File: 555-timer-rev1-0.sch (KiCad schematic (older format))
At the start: 10 parts, among them J1 Conn_01x02_Female, U1 SA555D

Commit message: Add bistable reset switch to schematic.
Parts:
- added JP?: SolderJumper_2_Open, Jumper:SolderJumper-2_P1.3mm_Open_TrianglePad1.0x1.5mm, symbol Jumper:SolderJumper_2_Open
- added R?: 220, Resistor_SMD:R_1206_3216Metric_Pad1.42x1.75mm_HandSolder, symbol Device:R
- added SW?: SW_Push, symbol Switch:SW_Push
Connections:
- net +5V: now also R?.1; no longer U1.4 (R)
- net GND: now also SW?.1
- new net: JP?.1 (A), R?.2, U1.4 (R)
- new net: JP?.2 (B), SW?.2
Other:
- moved on the sheet: C2
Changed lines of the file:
@@
 L Device:C C2
 U 1 1 5F27D81E
-P 4850 4450
-F 0 "C2" H 4965 4496 50  0000 L CNN
-F 1 "100pF" H 4965 4405 50  0000 L CNN
-F 2 "Capacitor_SMD:C_1206_3216Metric_Pad1.42x1.75mm_HandSolder" H 4888 4300 50  0001 C CNN
-F 3 "~" H 4850 4450 50  0001 C CNN
-	1    4850 4450
+P 4650 4450
+F 0 "C2" H 4765 4496 50  0000 L CNN
+F 1 "100pF" H 4765 4405 50  0000 L CNN
+F 2 "Capacitor_SMD:C_1206_3216Metric_Pad1.42x1.75mm_HandSolder" H 4688 4300 50  0001 C CNN
+F 3 "~" H 4650 4450 50  0001 C CNN
+	1    4650 4450
 	1    0    0    -1
 $EndComp
@@
 $EndComp
 Wire Wire Line
-	6000 3600 6000 3150
-Wire Wire Line
 	8050 5050 8050 5250
 Wire Wire Line
 	6500 4000 6750 4000
-Wire Wire Line
-	5500 4200 5350 4200
 $Comp
 L 555-timer-rev1-0:Conn_01x02_Female J1
@@
 $EndComp
 $Comp
-L power:GND #PWR?
+L power:GND #PWR0101
 U 1 1 5F2ACBC7
 P 8050 5950
-F 0 "#PWR?" H 8050 5700 50  0001 C CNN
+F 0 "#PWR0101" H 8050 5700 50  0001 C CNN
 F 1 "GND" H 8055 5777 50  0000 C CNN
 F 2 "" H 8050 5950 50  0001 C CNN
@@
 $EndComp
 $Comp
-L power:+5V #PWR?
+L power:+5V #PWR0102
 U 1 1 5F2AD001
-P 8050 3100
-F 0 "#PWR?" H 8050 2950 50  0001 C CNN
-F 1 "+5V" H 8065 3273 50  0000 C CNN
-F 2 "" H 8050 3100 50  0001 C CNN
-F 3 "" H 8050 3100 50  0001 C CNN
-	1    8050 3100
-	1    0    0    -1
-$EndComp
-Wire Wire Line
-	8050 3100 8050 3400
+P 8050 2850
+F 0 "#PWR0102" H 8050 2700 50  0001 C CNN
+F 1 "+5V" H 8065 3023 50  0000 C CNN
+F 2 "" H 8050 2850 50  0001 C CNN
+F 3 "" H 8050 2850 50  0001 C CNN
+	1    8050 2850
+	1    0    0    -1
+$EndComp
 Wire Wire Line
 	8050 5550 8050 5950
 $Comp
-L power:+5V #PWR?
+L power:+5V #PWR0103
 U 1 1 5F2B0EB0
 P 3200 4000
-F 0 "#PWR?" H 3200 3850 50  0001 C CNN
+F 0 "#PWR0103" H 3200 3850 50  0001 C CNN
 F 1 "+5V" H 3215 4173 50  0000 C CNN
 F 2 "" H 3200 4000 50  0001 C CNN
@@
 $EndComp
 $Comp
-L power:GND #PWR?
+L power:GND #PWR0104
 U 1 1 5F2B1695
 P 3200 4700
-F 0 "#PWR?" H 3200 4450 50  0001 C CNN
+F 0 "#PWR0104" H 3200 4450 50  0001 C CNN
 F 1 "GND" H 3205 4527 50  0000 C CNN
 F 2 "" H 3200 4700 50  0001 C CNN
@@
 	3200 4300 3200 4000
 $Comp
-L power:+5V #PWR?
+L power:+5V #PWR0105
 U 1 1 5F2B302B
-P 6000 3150
-F 0 "#PWR?" H 6000 3000 50  0001 C CNN
-F 1 "+5V" H 6015 3323 50  0000 C CNN
-F 2 "" H 6000 3150 50  0001 C CNN
-F 3 "" H 6000 3150 50  0001 C CNN
-	1    6000 3150
-	1    0    0    -1
-$EndComp
-$Comp
-L power:GND #PWR?
+P 6000 2850
+F 0 "#PWR0105" H 6000 2700 50  0001 C CNN
+F 1 "+5V" H 6015 3023 50  0000 C CNN
+F 2 "" H 6000 2850 50  0001 C CNN
+F 3 "" H 6000 2850 50  0001 C CNN
+	1    6000 2850
+	1    0    0    -1
+$EndComp
+$Comp
+L power:GND #PWR0106
 U 1 1 5F2B3448
-P 4850 4850
-F 0 "#PWR?" H 4850 4600 50  0001 C CNN
-F 1 "GND" H 4855 4677 50  0000 C CNN
-F 2 "" H 4850 4850 50  0001 C CNN
-F 3 "" H 4850 4850 50  0001 C CNN
-	1    4850 4850
-	1    0    0    -1
-$EndComp
-Wire Wire Line
-	4850 4600 4850 4850
+P 4650 4850
+F 0 "#PWR0106" H 4650 4600 50  0001 C CNN
+F 1 "GND" H 4655 4677 50  0000 C CNN
+F 2 "" H 4650 4850 50  0001 C CNN
+F 3 "" H 4650 4850 50  0001 C CNN
+	1    4650 4850
+	1    0    0    -1
+$EndComp
+Wire Wire Line
+	4650 4600 4650 4850
 Wire Wire Line
 	7250 4700 7250 4850
@@
 	7250 5350 7250 5400
 $Comp
-L power:GND #PWR?
+L power:GND #PWR0107
 U 1 1 5F2BFE55
 P 7250 5950
-F 0 "#PWR?" H 7250 5700 50  0001 C CNN
+F 0 "#PWR0107" H 7250 5700 50  0001 C CNN
 F 1 "GND" H 7255 5777 50  0000 C CNN
 F 2 "" H 7250 5950 50  0001 C CNN
@@
 	7250 5700 7250 5950
 $Comp
-L power:GND #PWR?
+L power:GND #PWR0108
 U 1 1 5F2C0AA3
 P 6000 4650
-F 0 "#PWR?" H 6000 4400 50  0001 C CNN
+F 0 "#PWR0108" H 6000 4400 50  0001 C CNN
 F 1 "GND" H 6005 4477 50  0000 C CNN
 F 2 "" H 6000 4650 50  0001 C CNN
@@
 	6000 4400 6000 4650
 $Comp
-L power:+5V #PWR?
+L power:+5V #PWR0109
 U 1 1 5F2C36D5
 P 7250 4100
-F 0 "#PWR?" H 7250 3950 50  0001 C CNN
+F 0 "#PWR0109" H 7250 3950 50  0001 C CNN
 F 1 "+5V" H 7265 4273 50  0000 C CNN
 F 2 "" H 7250 4100 50  0001 C CNN
@@
 Wire Wire Line
 	6500 4200 6500 5350
-$Comp
-L power:+5V #PWR?
-U 1 1 5F2C76F1
-P 5350 4200
-F 0 "#PWR?" H 5350 4050 50  0001 C CNN
-F 1 "+5V" V 5365 4328 50  0000 L CNN
-F 2 "" H 5350 4200 50  0001 C CNN
-F 3 "" H 5350 4200 50  0001 C CNN
-	1    5350 4200
-	0    -1   -1   0
-$EndComp
-Wire Wire Line
-	4850 4000 4850 4300
-Wire Wire Line
-	4850 4000 5500 4000
-Wire Wire Line
-	4500 3800 5500 3800
+Wire Wire Line
+	4650 4000 4650 4300
+Wire Wire Line
+	4400 3800 5500 3800
 Wire Wire Line
 	8050 4150 8050 4450
@@
 	6100 5350 6500 5350
 Connection ~ 6500 5350
+$Comp
+L power:+5V #PWR?
+U 1 1 5F2CD6A0
+P 5250 2850
+F 0 "#PWR?" H 5250 2700 50  0001 C CNN
+F 1 "+5V" H 5265 3023 50  0000 C CNN
+F 2 "" H 5250 2850 50  0001 C CNN
+F 3 "" H 5250 2850 50  0001 C CNN
+	1    5250 2850
+	1    0    0    -1
+$EndComp
+$Comp
+L Jumper:SolderJumper_2_Open JP?
+U 1 1 5F2CE483
+P 5250 5750
+F 0 "JP?" V 5204 5818 50  0000 L CNN
+F 1 "SolderJumper_2_Open" V 5295 5818 50  0000 L CNN
+F 2 "Jumper:SolderJumper-2_P1.3mm_Open_TrianglePad1.0x1.5mm" H 5250 5750 50  0001 C CNN
+F 3 "~" H 5250 5750 50  0001 C CNN
+	1    5250 5750
+	0    1    1    0
+$EndComp
+Wire Wire Line
+	5250 4200 5250 5600
+Connection ~ 5250 4200
+$Comp
+L Device:R R?
+U 1 1 5F2D3863
+P 5250 3350
+F 0 "R?" H 5320 3396 50  0000 L CNN
+F 1 "220" H 5320 3305 50  0000 L CNN
+F 2 "Resistor_SMD:R_1206_3216Metric_Pad1.42x1.75mm_HandSolder" V 5180 3350 50  0001 C CNN
+F 3 "~" H 5250 3350 50  0001 C CNN
+	1    5250 3350
+	1    0    0    -1
+$EndComp
+Wire Wire Line
+	5250 3500 5250 4200
+Wire Wire Line
+	5250 4200 5500 4200
+Wire Wire Line
+	4650 4000 5500 4000
+$Comp
+L Switch:SW_Push SW?
+U 1 1 5F2D850F
+P 5250 6250
+F 0 "SW?" V 5296 6202 50  0000 R CNN
+F 1 "SW_Push" V 5205 6202 50  0000 R CNN
+F 2 "" H 5250 6450 50  0001 C CNN
+F 3 "~" H 5250 6450 50  0001 C CNN
+	1    5250 6250
+	0    -1   -1   0
+$EndComp
+Wire Wire Line
+	5250 5900 5250 6050
+$Comp
+L power:GND #PWR?
+U 1 1 5F2D9CE9
+P 5250 6650
+F 0 "#PWR?" H 5250 6400 50  0001 C CNN
+F 1 "GND" H 5255 6477 50  0000 C CNN
+F 2 "" H 5250 6650 50  0001 C CNN
+F 3 "" H 5250 6650 50  0001 C CNN
+	1    5250 6650
+	1    0    0    -1
+$EndComp
+Wire Wire Line
+	5250 6450 5250 6650
+Wire Wire Line
+	8050 2850 8050 3400
+Wire Wire Line
+	6000 2850 6000 3600
+Wire Wire Line
+	5250 2850 5250 3200
 $EndSCHEMATC

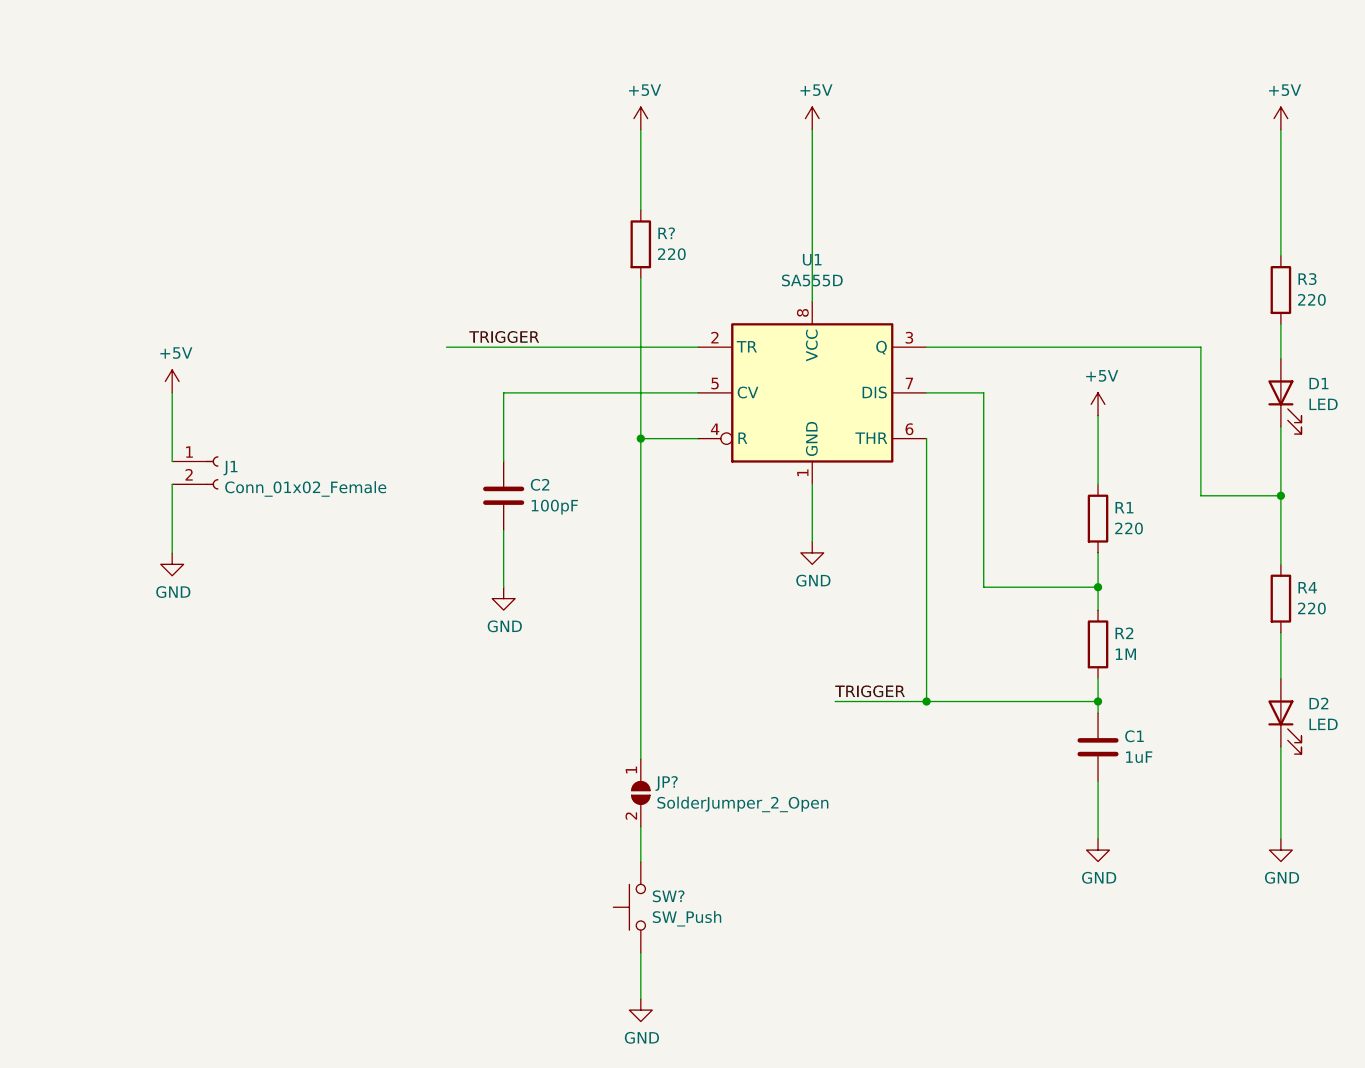
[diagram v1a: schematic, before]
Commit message: Add astable and bistable switches and jumpers.
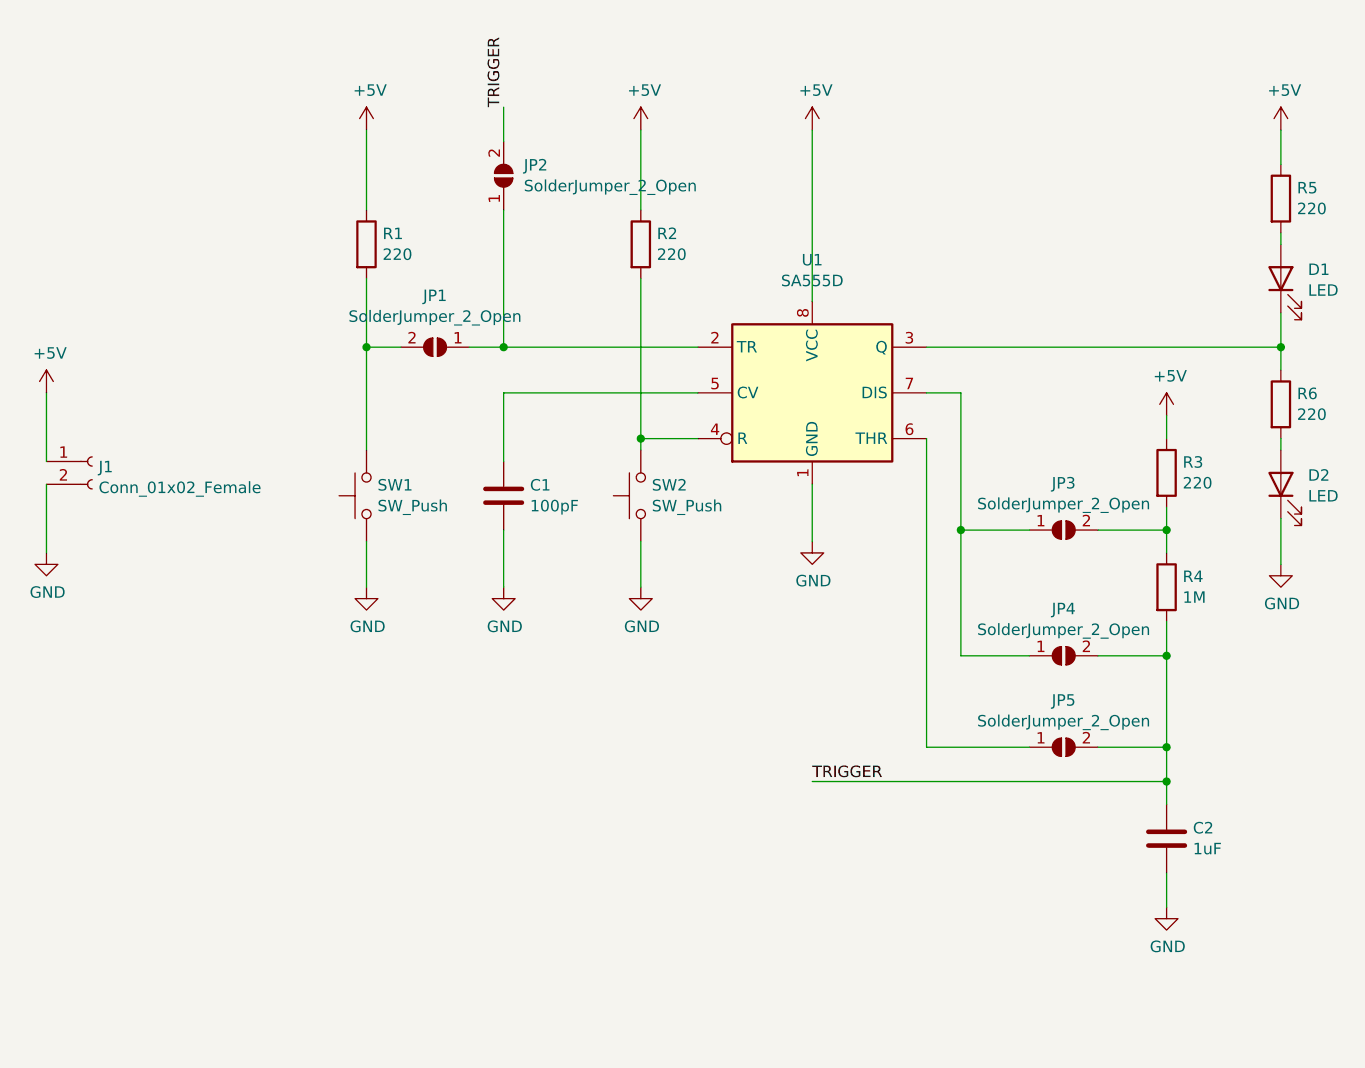
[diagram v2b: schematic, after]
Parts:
- removed JP?: SolderJumper_2_Open, Jumper:SolderJumper-2_P1.3mm_Open_TrianglePad1.0x1.5mm, symbol Jumper:SolderJumper_2_Open
- added JP1, JP2, JP3, JP4, JP5: SolderJumper_2_Open, Jumper:SolderJumper-2_P1.3mm_Open_TrianglePad1.0x1.5mm, symbol Jumper:SolderJumper_2_Open
- added R1: 220, Resistor_SMD:R_1206_3216Metric_Pad1.42x1.75mm_HandSolder, symbol Device:R
- added SW1: SW_Push, symbol Switch:SW_Push
- J1: footprint (none) -> Connector_PinSocket_2.54mm:PinSocket_1x02_P2.54mm_Vertical
- gave numbers to parts that had none: 2
- renumbered C2 to C1, C1 to C2, R1 to R3, R2 to R4, R3 to R5, R4 to R6
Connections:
- net +5V: now also R1.1
- net GND: now also SW1.1
- net TRIGGER: now also JP2.2 (B), JP4.2 (B), JP5.2 (B); no longer U1.2 (TR), U1.6 (THR)
- net at R2.2, U1.4 (R): now also SW2.2
- net at R3.2, R4.1: now also JP3.2 (B); no longer U1.7 (DIS)
- new net: JP1.1 (A), JP2.1 (A), U1.2 (TR)
- new net: JP5.1 (A), U1.6 (THR)
- new net: JP3.1 (A), JP4.1 (A), U1.7 (DIS)
- new net: JP1.2 (B), R1.2, SW1.2
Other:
- moved on the sheet: C2, D1, D2, J1, R3, R4, R5, R6, SW2
